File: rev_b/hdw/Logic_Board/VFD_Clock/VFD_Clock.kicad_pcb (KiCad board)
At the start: 4 copper layers, 200 x 50 mm, 358 parts, among them J1501 PICKIT4, J1801 I2C, J1802 USB UART, J201 +12V IN, J2401 USB_B_Mini, J3001 DSP_IO_Connector, Q1001 IRFL214TRPBF, Q1301 BSS214NW, Q1302 ZXMS6004FFTA, Q1304 BSS214NW, Q1306 ZXMS6004FFTA, Q1307 BSS214NW, Q1308 ZXMS6004FFTA, Q1501 BSS214NW, Q1801 BSS214NW, Q201 IPC100N04S51R7ATMA1, Q202 IPC100N04S51R7ATMA1, SW1501 MRST, U1001 TLV6700, U1002 LT3757, U1101 MCP9804, U1103 LTC4151DD, U1401 PIC32MZ2048EFG100_IPT, U1801 LTC6900, U1802 74LVC1G97, U1803 MCP9804, U2001 74LVC1G97, U2003 74LVC1G97, U2004 74LVC1G97, U2006 74LVC1G97, U201 LTC4365DDB, U2101 TPS71533, U2102 74LVC1G97, U2103 74LVC1G97, U2104 74LVC1G97, U2105 74LVC1G97, U2106 74LVC1G97, U2107 74LVC1G97, U2108 74LVC1G97, U2201 TCA9803, U2301 DS1683, U2401 TLV6700, U2402 FT234XD, U2403 TPD3S014DBVR, U2404 SN74AVC2T245, U2601 INA219BxDCN, U2602 MCP9804, U2801 74VHC541, U2802 74VHC541, U2803 74LVC1G97, U2804 74LVC1G97, U2901 TCA9803, U2902 74VHC541, U301 INA219BxDCN, U302 MCP9804, U401 TPS62130, U502 MCP9804, U503 INA219BxDCN, U601 TPS62130, U702 MCP9804, U703 INA219BxDCN, U801 TPS62130, U902 MCP9804, U903 INA219BxDCN, X1701 ASE-8.000MHz, X1702 ECS-327KE

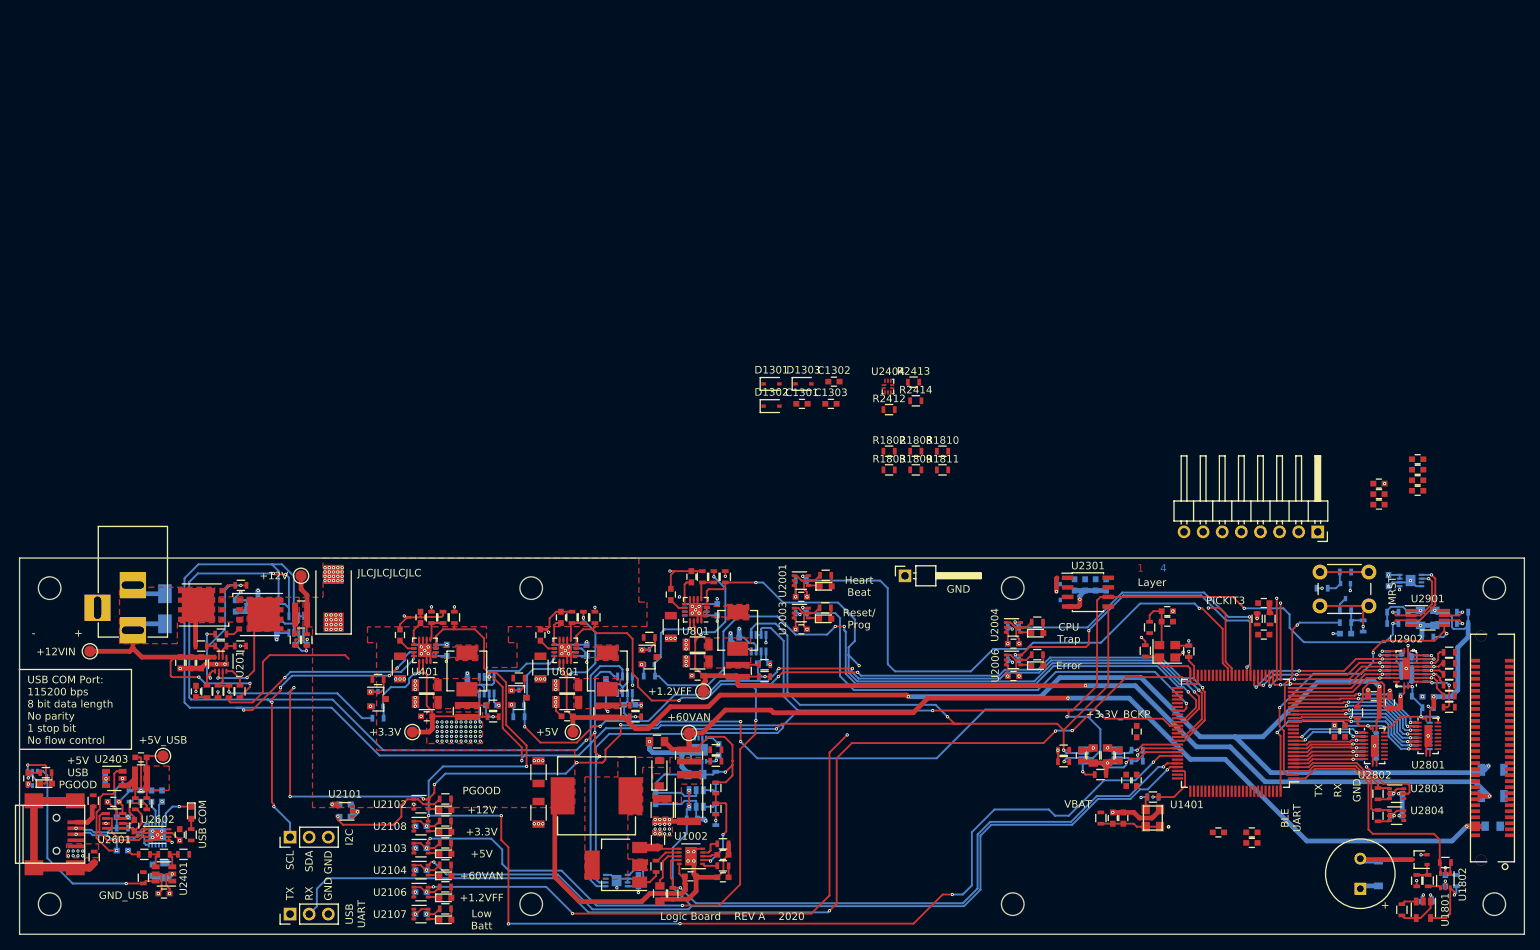
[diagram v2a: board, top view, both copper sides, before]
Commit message: Finished rev B schematic, pulled into PCB
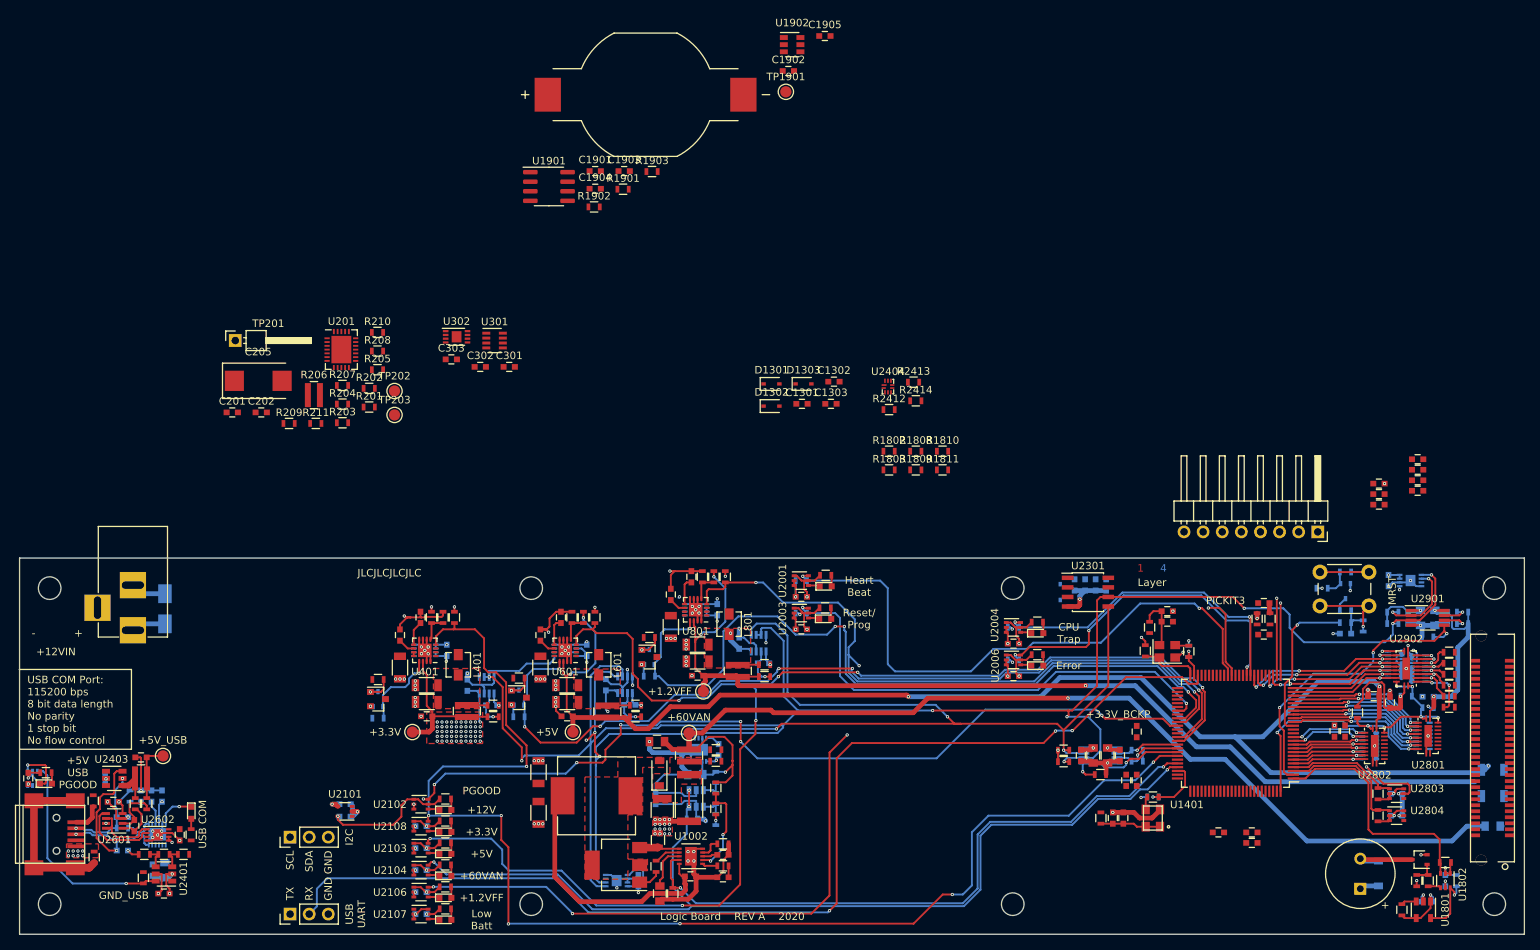
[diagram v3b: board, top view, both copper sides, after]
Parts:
- removed C203: 1nF, Capacitors_SMD:C_0603
- removed C204: 0.1uF, Capacitors_SMD:C_0603
- removed Q201, Q202: IPC100N04S51R7ATMA1, TO_SOT_Packages_SMD:TDSON-8-1
- removed R212: 10, Resistors_SMD:R_0603
- added BT1902: CR1616_Holder, Custom Footprints Library:BAT_BU1632SM-JJ-GTR, F.Cu at (117.5, 4.70)
- added C1901: 0.1uF, Capacitors_SMD:C_0603, F.Cu at (110.8, 14.8)
- added C1902: 10uF, Capacitors_SMD:C_0603, F.Cu at (136.5, 1.55)
- added C1903: 0.1uF, Capacitors_SMD:C_0603, F.Cu at (114.7, 14.8)
- added C1904: 0.1uF, Capacitors_SMD:C_0603, F.Cu at (110.8, 17.2)
- added C1905: 0.1uF, Capacitors_SMD:C_0603, F.Cu at (141.4, -3.10)
- added R1901: 1.07M, Resistors_SMD:R_0603, F.Cu at (114.5, 17.3)
- added R1902: 220k, Resistors_SMD:R_0603, F.Cu at (110.7, 19.6)
- added R1903: 10k, Resistors_SMD:R_0603, F.Cu at (118.4, 14.9)
- added TP1901: TP, Custom Footprints Library:Test_Point, F.Cu at (136.2, 4.32)
- added U1901: DS3231MZ, Package_SO:SOIC-8_3.9x4.9mm_P1.27mm, F.Cu at (104.7, 16.9)
- added U1902: TLV6700, TO_SOT_Packages_SMD:SOT-23-6, F.Cu at (137.0, -1.95)
- C201: value 0.1uF -> 10nF
- C202: value 10nF -> 0.1uF
- C301, C302, C303, U301, U302: moved to F.Cu
- L401, L601, L801: value 2.2u -> 2.2uH; footprint Inductors_SMD:L_Vishay_IHLP-2020 -> Inductors_SMD:L_Vishay_IHLP-1212
- R201: value 6.04M -> 51.1k
- R202: value 86.6k -> 1.15k
- R203: value 243k -> 5.11k
- R204: value 100k -> 10k
- R206: value 10 -> 0.02; footprint Resistors_SMD:R_0603 -> Resistors_SMD:R_0612
- R207: value 13.7k -> 10k
- R208: value 5.23k -> 13k
- R209: value 5.1k -> 5.11k
- R211: value 0.02 -> 10k; footprint Resistors_SMD:R_0612 -> Resistors_SMD:R_0603
- TP202, TP203: value TP -> TP_Pad
- U201: value LTC4365DDB -> TPS26600RHFT; footprint Housings_DFN_QFN:DFN-8-1EP_2x3mm_Pitch0.5mm -> Housings_DFN_QFN:QFN-24-1EP_4x5mm_Pitch0.5mm
- U401, U601, U801: value TPS62130 -> TPS62150A; footprint Housings_DFN_QFN:QFN-16-1EP_3x3mm_Pitch0.5mm -> Package_DFN_QFN:QFN-16-1EP_3x3mm_P0.5mm_EP1.8x1.8mm
- moved TP201 94.3 mm to (63.0, 37.4)
- moved TP202 53.3 mm to (84.2, 44.1)
- moved R208 50.0 mm to (81.9, 38.8), turned to 0 degrees
- moved C301 46.1 mm to (99.4, 40.9), turned to 0 degrees
- moved U301 46.0 mm to (97.5, 37.4), turned to 0 degrees
- moved U201 44.8 mm to (77.1, 38.6), turned to 0 degrees
- moved U302 44.5 mm to (92.4, 36.9), turned to 0 degrees
- moved C302 43.9 mm to (95.6, 40.9), turned to 0 degrees
- moved C303 43.5 mm to (91.7, 39.9), turned to 0 degrees
- moved R207 43.4 mm to (77.3, 43.3), turned to 0 degrees
- moved R210 42.3 mm to (81.9, 36.3), turned to 0 degrees
- moved R204 40.5 mm to (77.3, 45.8), turned to 0 degrees
- moved R202 39.5 mm to (80.8, 43.7)
- moved R201 38.8 mm to (80.8, 46.2)
- moved R209 37.3 mm to (70.2, 48.4), turned to 0 degrees
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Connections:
- C201 pad 1: +12Vin -> Net-(C201-Pad1)
- C201 pad 2: GND -> Net-(C201-Pad2)
- R203 pad 2: GND -> Net-(C201-Pad2)
- R205 pad 1: Net-(R205-Pad1) -> POS12_SNS+
- R205 pad 2: Net-(Q201-Pad4) -> Net-(R205-Pad2)
- R206 pad 1: Net-(Q202-Pad4) -> Net-(R205-Pad2)
- R206 pad 2: Net-(R205-Pad1) -> +12V
- R207 pad 1: +12V -> Net-(R207-Pad1)
- R207 pad 2: POS12_PGOOD -> Net-(C201-Pad2)
- R208 pad 1: POS12_PGOOD -> +12V
- R208 pad 2: GND -> POS12_PGOOD
- R209 pad 1: Net-(R205-Pad1) -> POS12_PGOOD
- R209 pad 2: Net-(C204-Pad1) -> GND
- R210 pad 1: POS12_SNS+ -> POS12_SNS-
- R210 pad 2: Net-(Q202-Pad5) -> +12V
- R211 pad 1: Net-(Q202-Pad5) -> Net-(R211-Pad1)
- R211 pad 2: +12V -> Net-(C201-Pad2)
- U201 pad 1: GND -> Net-(U201-Pad1)
- U201 pad 2: Net-(R202-Pad2) -> Net-(U201-Pad2)
- U201 pad 3: Net-(R201-Pad2) -> Net-(U201-Pad3)
- U201 pad 4: +12Vin -> Net-(U201-Pad4)
- U201 pad 5: Net-(R205-Pad1) -> Net-(U201-Pad5)
- U201 pad 6: Net-(Q202-Pad5) -> Net-(U201-Pad6)
- U201 pad 7: POS12_PGOOD -> Net-(U201-Pad7)
- U201 pad 8: Net-(R204-Pad2) -> +12Vin
- U201 pad 9: GND -> +12Vin
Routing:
- net I2C_SCL: track 323.2 -> 187.7 mm, vias 15 -> 8
- net I2C_SDA: track 381.4 -> 262.2 mm, vias 10 -> 8
- net POS12_PGOOD: track 172.7 -> 114.0 mm, vias 10 -> 7
- net +12Vin: track 45.9 -> 4.61 mm, vias 2 -> 0
- net +12V: track 73.6 -> 43.8 mm, vias 17 -> 1
- net GND: track 307.4 -> 281.5 mm, vias 177 -> 150
- net Net-(R205-Pad1): track 22.0 -> 0.00 mm, vias 3 -> 0
- net Net-(Q202-Pad5): track 15.2 -> 0.00 mm, vias 2 -> 0
- net +3V3: track 189.5 -> 182.3 mm, vias 93 -> 90
- net +1.2VFF: track 139.6 -> 134.5 mm, vias 4 -> 3
- net POS12_SNS+: track 4.83 -> 0.00 mm, vias 1 -> 0
- net POS12_SNS-: track 4.28 -> 0.00 mm, vias 1 -> 0
- net Net-(R204-Pad2): track 3.16 -> 0.00 mm
- net Net-(R201-Pad2): track 2.80 -> 0.00 mm
- net Net-(R202-Pad2): track 2.80 -> 0.00 mm
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- removed copper zone on F.Cu, net +12V
- removed copper zone on F.Cu, net +12Vin
- removed copper zone on F.Cu, net +5V_USB
- removed copper zone on F.Cu, net Net-(L401-Pad1)
- removed copper zone on F.Cu, net Net-(L601-Pad1)
- removed copper zone on F.Cu, net Net-(L801-Pad1)
- removed copper zone on F.Cu, net Net-(Q201-Pad1)
- removed copper zone on F.Cu, net Net-(Q202-Pad5)
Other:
- board text removed: "BLE UART"
- board text removed: "VBAT"

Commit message: More sch work, ran ERC
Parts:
- removed R2204, R2205, R2901, R2902, R2905, R2906: 10k, Resistors_SMD:R_0603
- C1901, C1905: moved to B.Cu
- R2401: moved to F.Cu
- R2406, R2410: value 100 -> 10
- moved R2401 120.6 mm to (147.7, 28.5), turned to 90 degrees
- moved U1902 110.8 mm to (169.1, 104.1), turned to 270 degrees
- moved C1905 110.7 mm to (169.1, 104.1), turned to 90 degrees
- moved C1901 108.9 mm to (195.4, 83.6)
- moved R1903 103.9 mm to (171.8, 104.1), turned to 90 degrees
- moved U1901 102.7 mm to (169.2, 96.9), turned to 180 degrees
- moved C1904 102.6 mm to (174.6, 97.5)
- moved R1902 101.2 mm to (166.5, 104.1), turned to 270 degrees
- moved R1901 100.4 mm to (165.0, 104.1), turned to 90 degrees
- moved C1902 97.7 mm to (162.9, 95.6), turned to 90 degrees
- moved BT1902 97.5 mm to (145.4, 98.2), turned to 180 degrees
- moved C1903 94.8 mm to (164.5, 95.6), turned to 90 degrees
- moved TP1901 92.2 mm to (161.8, 92.9)
- moved C1606 48.2 mm to (184.2, 89.3), turned to 270 degrees
- moved C1605 47.9 mm to (193.7, 100.6)
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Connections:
- C2201 pad 1: +3.3V_BCKP -> +3V3
- C2202 pad 1: +3.3V_BCKP -> +3V3
- L1701 pad 2: +3.3V_BCKP -> +3V3
- L1702 pad 2: +3.3V_BCKP -> +3V3
- R2201 pad 1: +3.3V_BCKP -> +3V3
- R2202 pad 1: +3.3V_BCKP -> +3V3
- R2406 pad 1: +5V_USB -> POS5_USB_SNS-
- R2406 pad 2: POS5_USB_SNS- -> +5V_USB
- R2410 pad 1: Net-(R2407-Pad2) -> POS5_USB_SNS+
- R2410 pad 2: POS5_USB_SNS+ -> Net-(R2407-Pad2)
- U1401 pad 30: +3.3VA -> +3.3VA_MZ
- U1401 pad 31: GNDA -> GNDA_MZ
- U1401 pad 42: VBAT_ADC_Enable -> Backup_RTC_Config
- U1401 pad 43: Net-(U1401-Pad43) -> TOF_Config
- U1401 pad 44: Net-(U1401-Pad44) -> Telemetry_Config
- U2201 pad 1: +3.3V_BCKP -> +3V3
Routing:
- net +1.2VFF: track 134.5 -> 77.5 mm
- net +5V: track 234.9 -> 215.5 mm
- net POS5_USB_SNS-: track 7.06 -> 2.14 mm
- net +3V3: track 182.3 -> 177.7 mm, vias 90 -> 88
- net +3.3V_BCKP: track 4.47 -> 0.00 mm, vias 1 -> 0
- net I2C_SDA: track 262.2 -> 257.9 mm, vias 8 -> 7
- net I2C_SCL: track 187.7 -> 183.6 mm, vias 8 -> 7
- net POS5_USB_SNS+: track 5.51 -> 1.76 mm
- net I2C_DSP_SDA: track 3.37 -> 0.00 mm, vias 1 -> 0
- net I2C_DSP_SCL: track 3.37 -> 0.00 mm, vias 1 -> 0
- net Net-(R2407-Pad2): track 4.74 -> 2.16 mm
- net +5V_USB: track 10.8 -> 8.24 mm
- net GND: track 281.5 -> 281.3 mm, vias 150 -> 148
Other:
- board text added: "+VBAT"
- board text added: "PICKIT4"
- board text removed: "+3.3V_BCKP"
- board text removed: "Components: 515 Track Segments: 3535 Pads: 1676 Vias: 836 Nets: 318"
- board text removed: "GND_USB"
- board text removed: "PICKIT3"

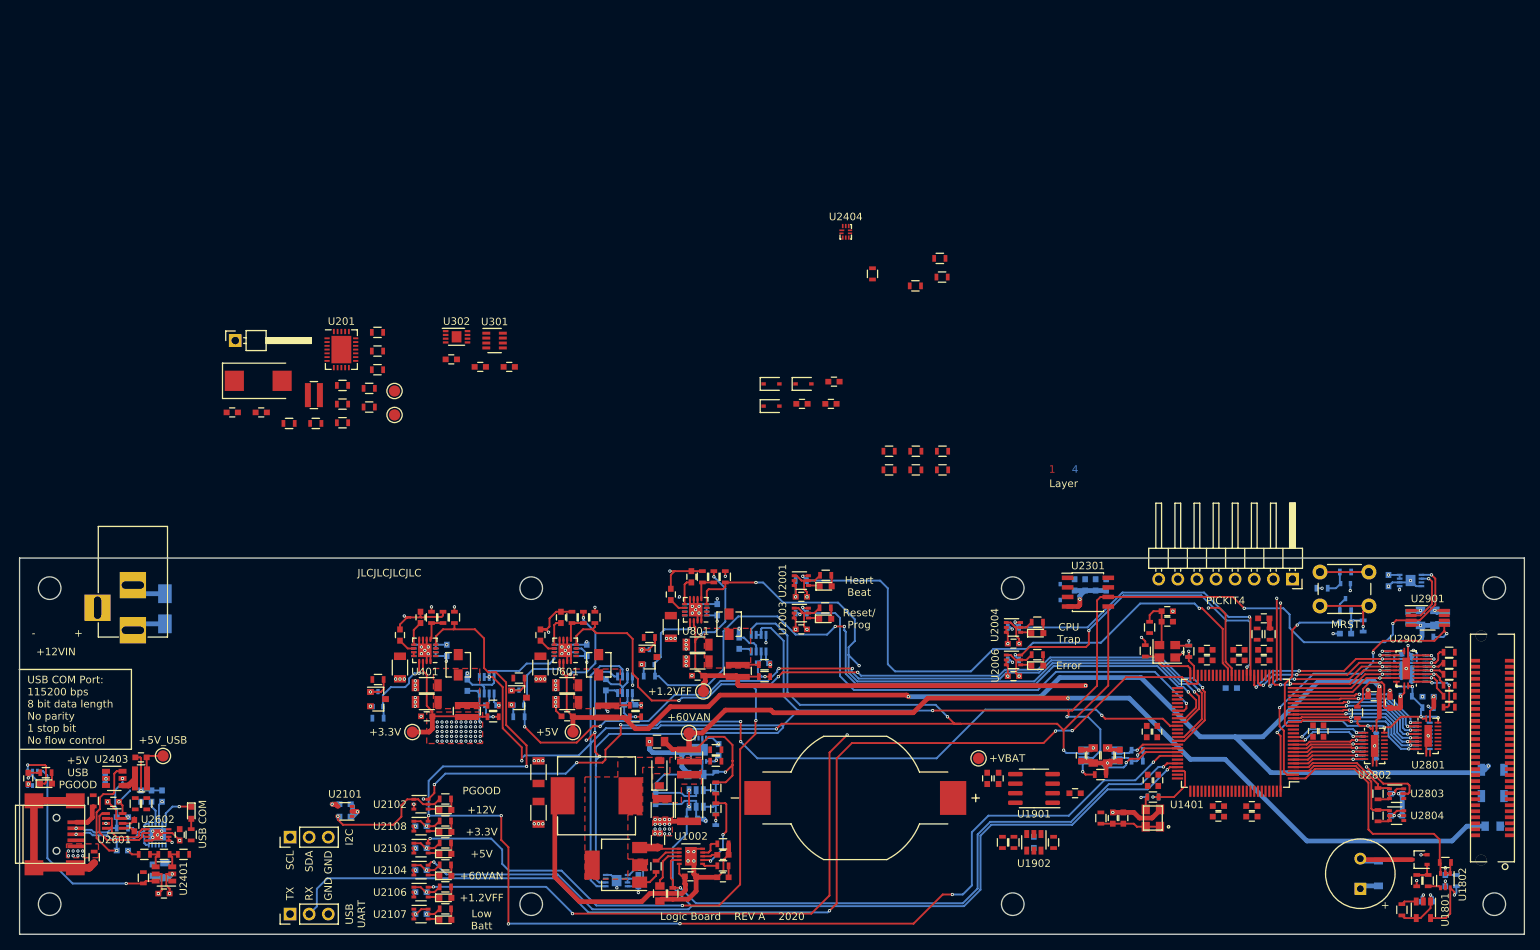
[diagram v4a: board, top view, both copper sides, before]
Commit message: placed more new parts on board
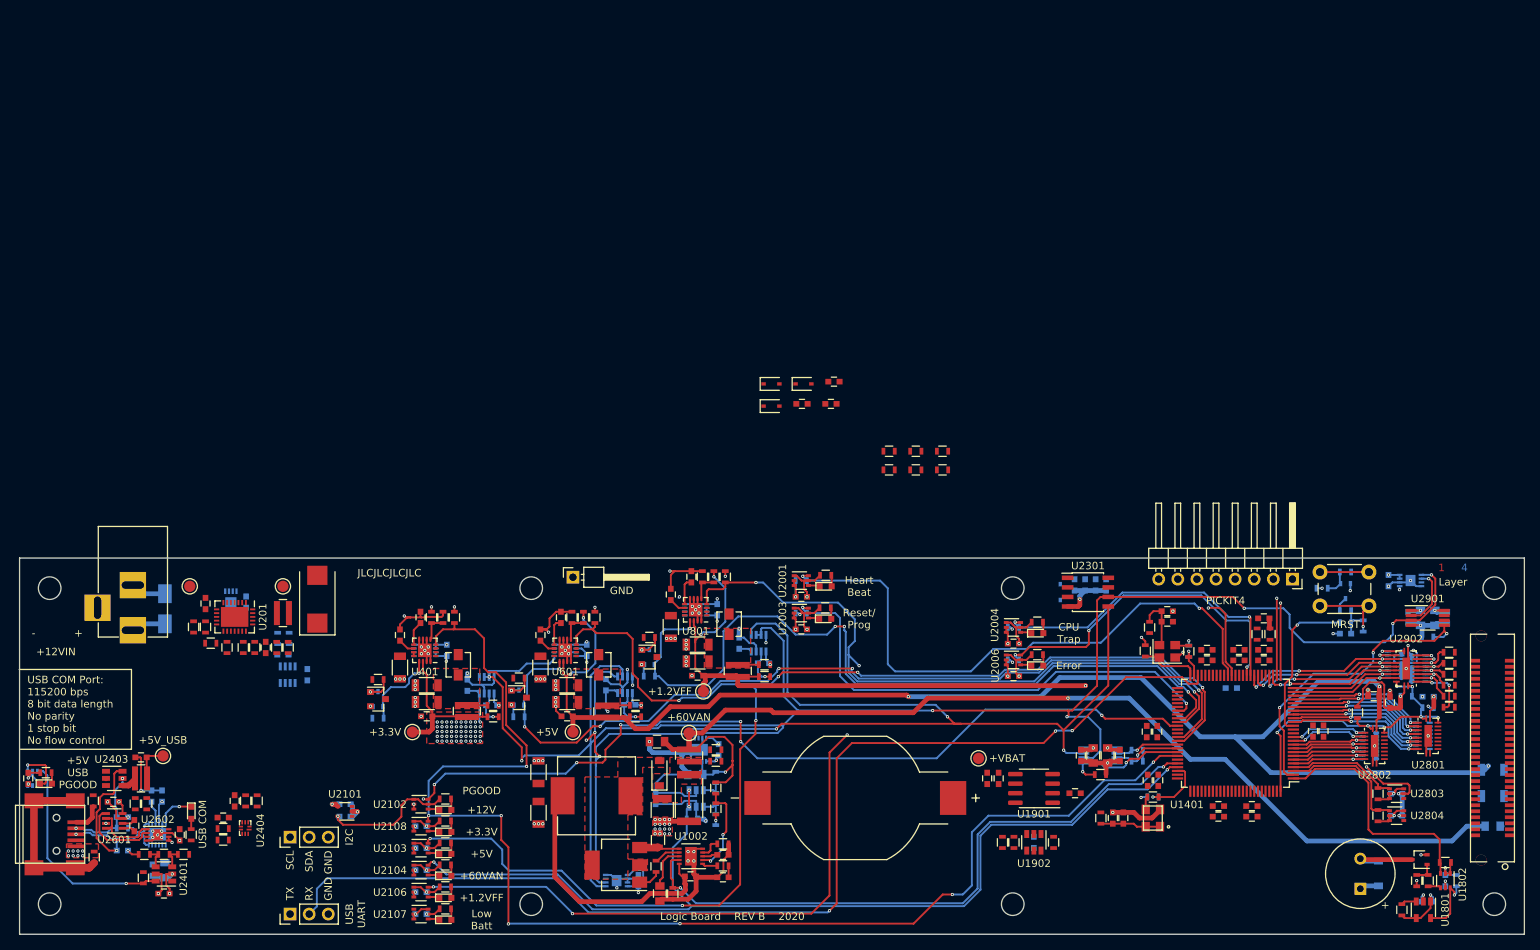
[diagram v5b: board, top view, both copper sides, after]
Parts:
- C2401, C2410: moved to F.Cu
- C301, C302, C303, R205, R210, U301, U302: moved to B.Cu
- moved R2413 121.7 mm to (61.4, 102.2)
- moved R2414 121.4 mm to (61.4, 103.8)
- moved U2404 112.5 mm to (64.3, 102.2), turned to 180 degrees
- moved R2412 112.3 mm to (64.4, 98.6), turned to 270 degrees
- moved R2401 107.7 mm to (65.9, 98.6), turned to 270 degrees
- moved TP201 54.8 mm to (107.9, 68.8)
- moved U301 52.2 mm to (70.0, 81.8), turned to 270 degrees
- moved C301 48.7 mm to (69.3, 79.1)
- moved C302 46.9 mm to (72.6, 81.8), turned to 270 degrees
- moved U302 46.3 mm to (62.4, 72.1), turned to 90 degrees
- moved R210 42.3 mm to (70.2, 77.0), turned to 90 degrees
- moved C303 42.2 mm to (64.5, 72.1), turned to 270 degrees
- moved R208 41.1 mm to (70.0, 78.2), turned to 90 degrees
- moved R202 38.5 mm to (59.1, 75.4), turned to 270 degrees
- moved U201 38.3 mm to (62.9, 74.1), turned to 270 degrees
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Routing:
- net +3V3: track 177.7 -> 175.6 mm
- net GND: track 281.3 -> 280.5 mm, vias 148 -> 147
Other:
- board text added: "Logic Board REV B 2020"
- board text removed: "Logic Board REV A 2020"
